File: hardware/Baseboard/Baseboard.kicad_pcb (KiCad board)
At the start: 2 copper layers, 160 x 160 mm, 75 parts, among them IC1 74HC00, IC10 W65C22, IC11 74HC148, IC2 W65C02, IC3 74HC138, IC4 SYSTEM ROM, IC5 RAM, IC6 W65C22, IC7 W65C51, IC8 TL7702A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

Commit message: Working on PCB
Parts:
- removed C19, C4: 100nF, Capacitor_THT:C_Rect_L4.0mm_W2.5mm_P2.50mm
- removed R10: 10k, Resistor_THT:R_Axial_DIN0207_L6.3mm_D2.5mm_P7.62mm_Horizontal
- removed SW6: CLOCK, Button_Switch_THT:SW_PUSH_6mm_H4.3mm
- added C20: 100nF, Capacitor_THT:C_Rect_L4.0mm_W2.5mm_P2.50mm, F.Cu at (271.8, 181.1)
- added R11: 10k, Resistor_THT:R_Axial_DIN0207_L6.3mm_D2.5mm_P7.62mm_Horizontal, F.Cu at (275.3, 188.7)
- added SW8: FT232 RESET, Button_Switch_THT:SW_PUSH_6mm_H4.3mm, F.Cu at (283.5, 181.7)
- added X5: GND, Connector_PinHeader_2.54mm:PinHeader_1x01_P2.54mm_Vertical, F.Cu at (172.0, 56.1)
- added X6: EXT. CLOCK, Connector_Coaxial:MMCX_Molex_73415-1471_Vertical, F.Cu at (207.5, 161.0)
- moved SW7 5.85 mm to (225.6, 158.8), turned to 180 degrees
- moved SW5 2.02 mm to (291.3, 149.9)
- moved XTAL1 0.79 mm to (226.3, 150.6)
- moved IC11 0.38 mm to (180.3, 84.1)
- moved RN3 0.38 mm to (198.1, 72.4)
- moved R1 0.27 mm to (176.7, 84.3)
- moved IC2 0.25 mm to (243.3, 110.0)
- moved IC3 0.13 mm to (186.7, 138.9)
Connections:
- net /IO/~CarrierDetect renamed /IO/~DCD
- net /Processor/CLOCK_OSC renamed /Processor/CLOCK_INT
- net /Processor/CTS renamed /Processor/~CTS
- net /Processor/~ModemReady renamed /Processor/~DSR
- net /USB/CTS renamed /USB/~CTS
- IC7 pad 11: /IO/~TerminalReady -> /USB/~DSR
- IC9 pad 19: /IO/~Reset -> /Supply/~Reset_FT232
- IC9 pad 9: (no net) -> /USB/~DSR
- SW7 pad 3: /Processor/CLOCK_BTN -> /Processor/CLOCK_EXT
- X3 pad 26: /IO/~TerminalReady -> /IO/RDY
- X3 pad 28: /IO/RDY -> /IO/Sync
- X3 pad 30: /IO/Sync -> (no net)
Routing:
- net /Processor/CLOCK_BTN: track 99.7 -> 0.00 mm
- net /IO/~TerminalReady: track 53.0 -> 0.00 mm, vias 2 -> 0
- net /IO/~Reset: track 348.3 -> 304.4 mm, vias 7 -> 5
- net /Supply/~Reset_FT232: track 0.00 -> 32.9 mm, vias 0 -> 1
- net /USB/~DSR: track 0.00 -> 31.8 mm
- net /Processor/CLOCK_EXT: track 0.00 -> 14.0 mm
- net /IO/A2: track 361.1 -> 372.6 mm
- net /IO/A1: track 423.7 -> 435.3 mm
- net /IO/A0: track 419.2 -> 430.7 mm
- net /IO/A3: track 363.8 -> 375.4 mm
- net /Processor/~CS_VIA_1: track 101.1 -> 89.9 mm, vias 3 -> 2
- net /IO/~DCD: track 29.3 -> 23.5 mm, vias 1 -> 0
- net +5V: track 40.8 -> 35.6 mm
- net /Processor/CLOCK_INT: track 21.7 -> 26.2 mm
- net /Processor/~DSR: track 54.5 -> 50.3 mm
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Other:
- board text added: "Baseboard 1.0"
- board text added: "EXT"
- board text added: "INT"
- board text removed: "BTN"
- board text removed: "Baseboard 1.1"
- board text removed: "OSC"

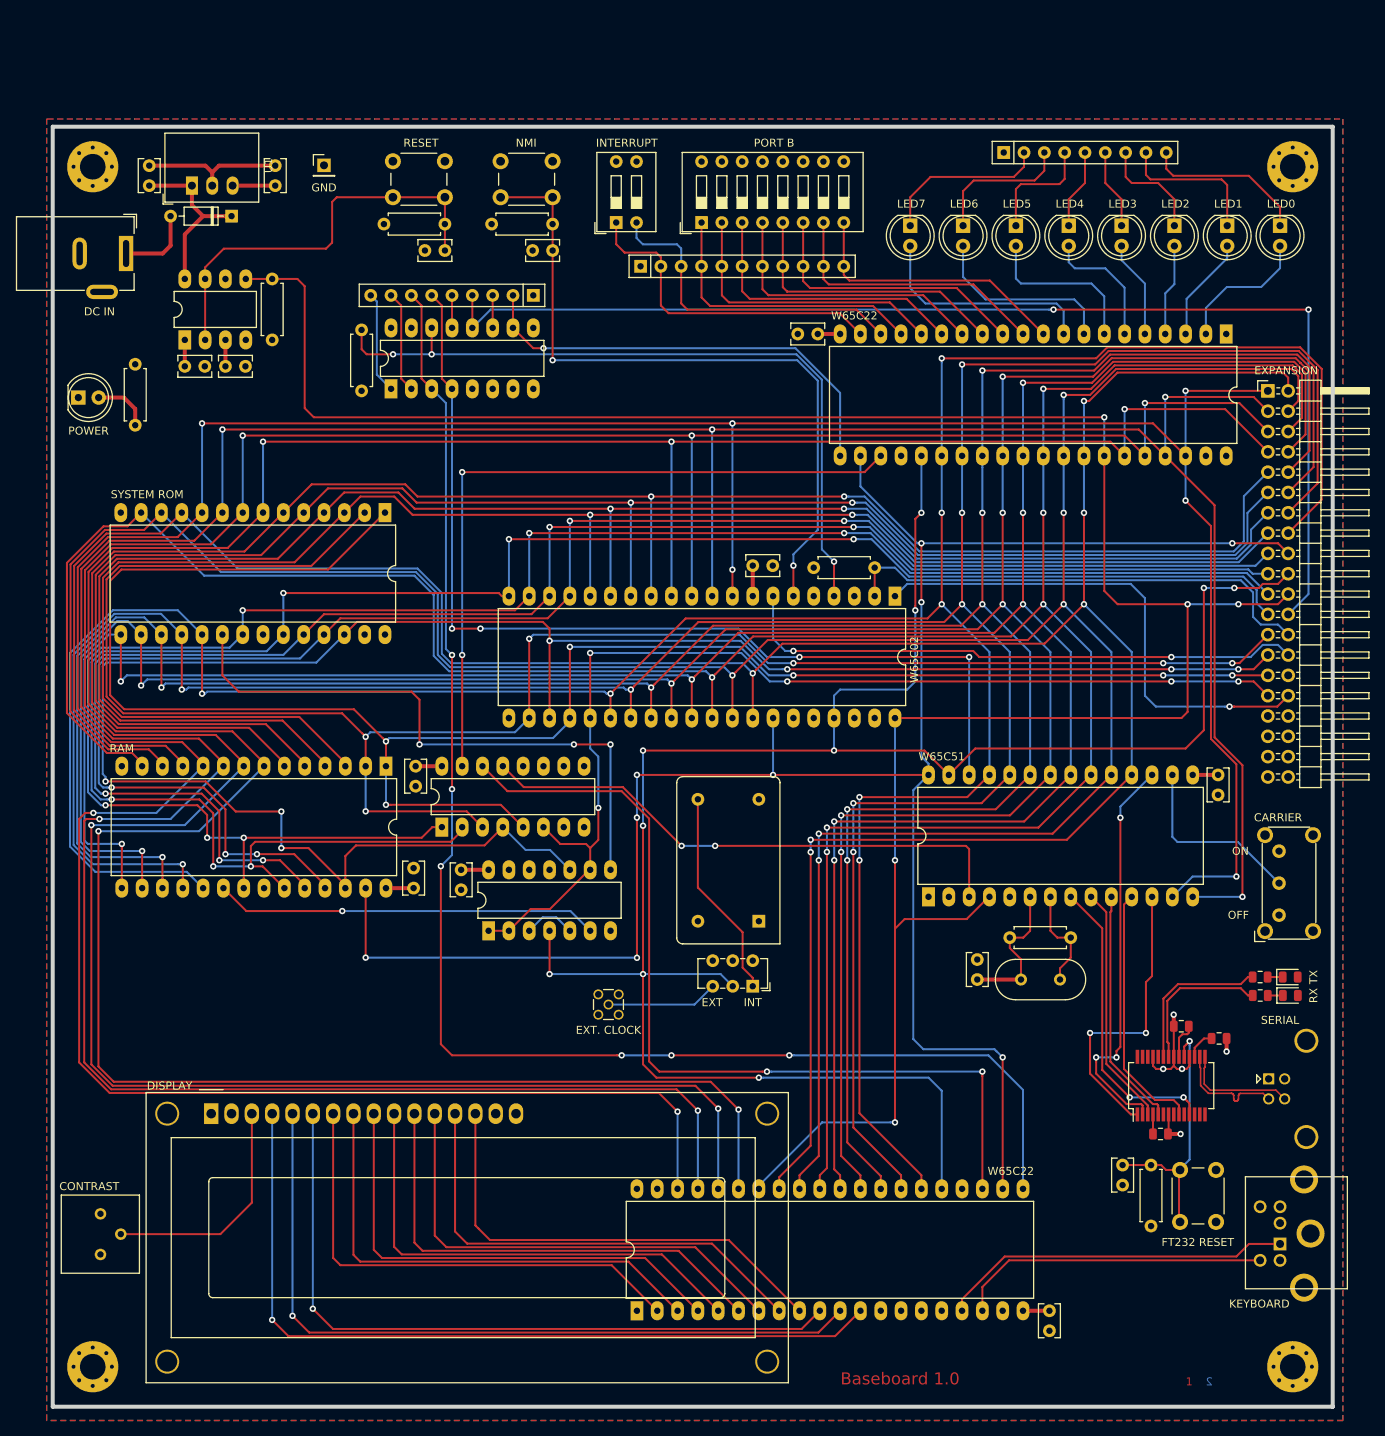
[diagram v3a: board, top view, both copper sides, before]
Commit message: Add pull up resistors for PS/2, add LCD backlight switch
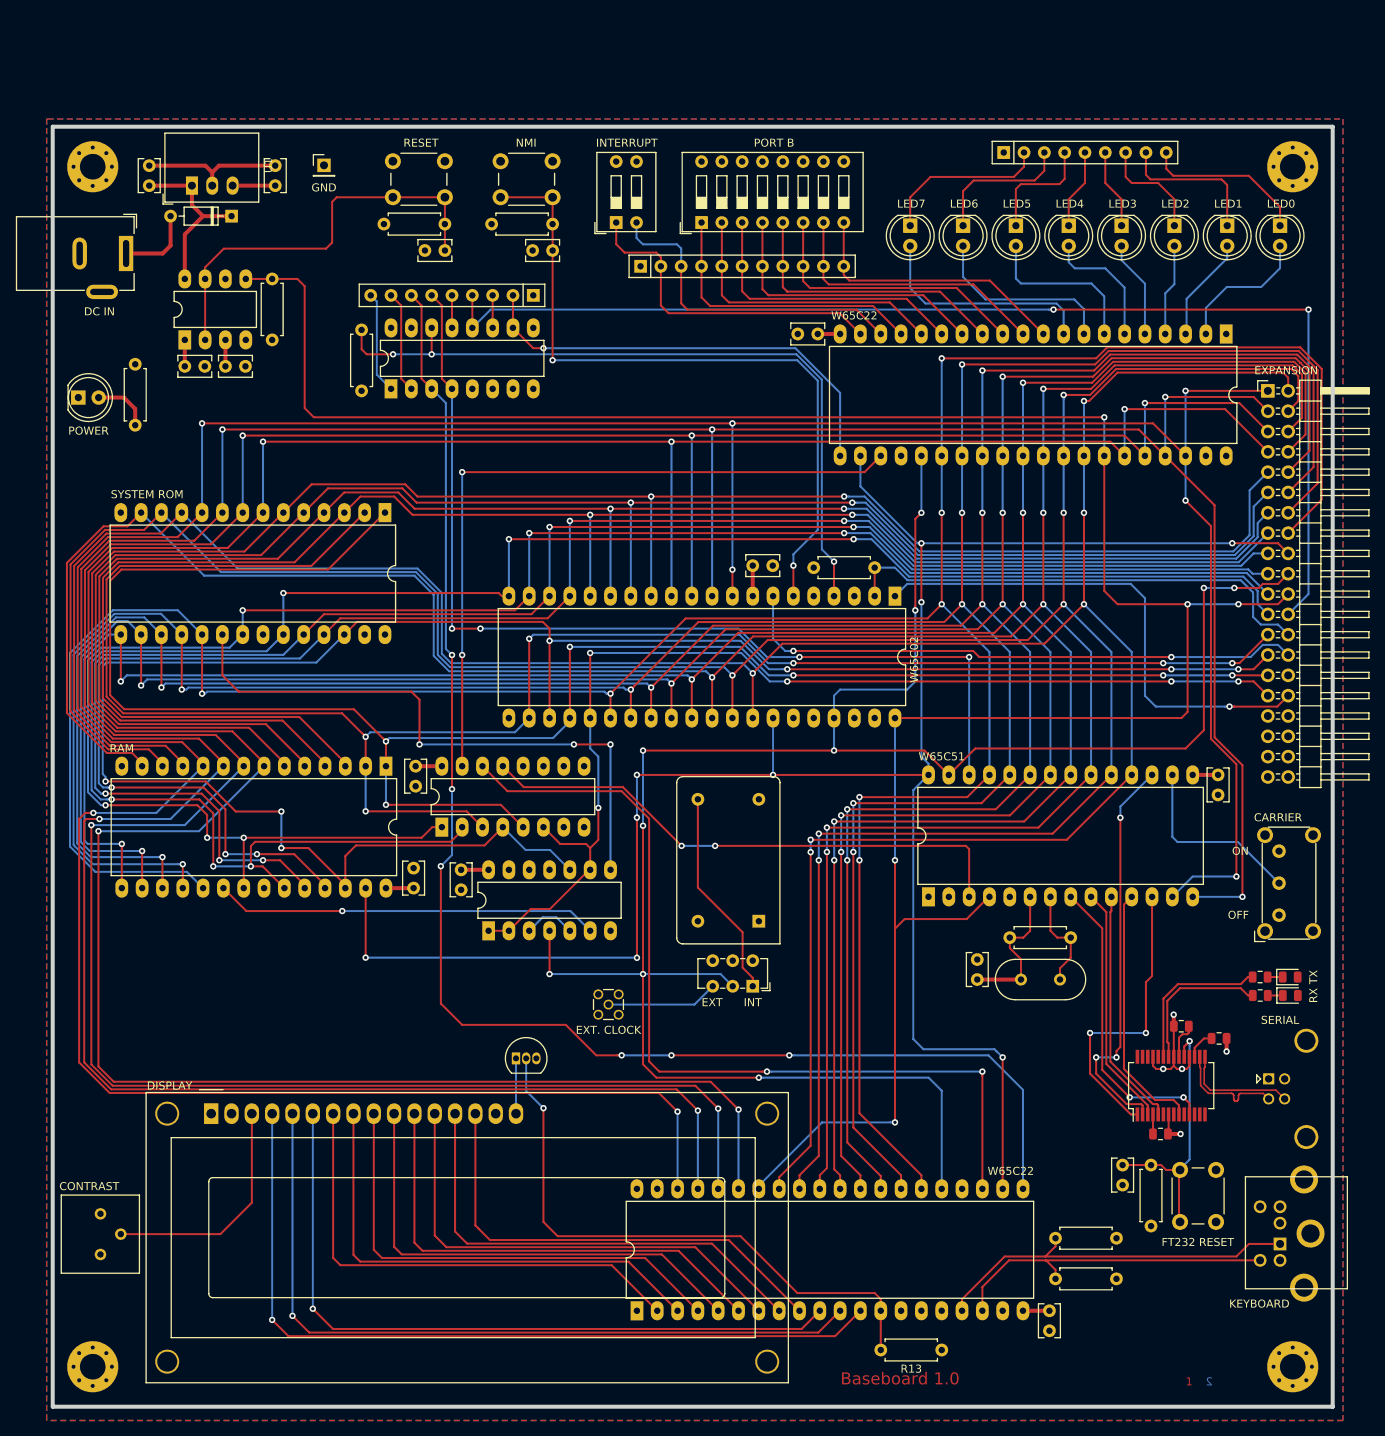
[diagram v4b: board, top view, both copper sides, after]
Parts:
- added R10: 10k, Resistor_THT:R_Axial_DIN0207_L6.3mm_D2.5mm_P7.62mm_Horizontal, F.Cu at (271.0, 195.3)
- added R12: 10k, Resistor_THT:R_Axial_DIN0207_L6.3mm_D2.5mm_P7.62mm_Horizontal, F.Cu at (271.0, 190.2)
- added R13: 4,7k, Resistor_THT:R_Axial_DIN0207_L6.3mm_D2.5mm_P7.62mm_Horizontal, F.Cu at (249.2, 204.2)
- added T1: BC546, Package_TO_SOT_THT:TO-92_Inline, F.Cu at (196.0, 167.8)
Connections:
- DS1 pad 16: GND -> Net-(DS1-Pad16)
- IC10 pad 13: (no net) -> /LCD / PS2/LCD11
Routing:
- net /LCD / PS2/LCD11: track 0.00 -> 73.9 mm, vias 0 -> 1
- net Net-(DS1-Pad16): track 0.00 -> 6.91 mm
- net /IRQ/~IRQ_VIA_2: track 183.8 -> 180.8 mm
- net /LCD / PS2/PS21: track 44.1 -> 46.9 mm
- net /LCD / PS2/PS20: track 39.1 -> 41.9 mm
- net /IO/A7: track 214.6 -> 214.1 mm
